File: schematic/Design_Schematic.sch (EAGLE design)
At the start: 8 parts, among them IC1 DS1307

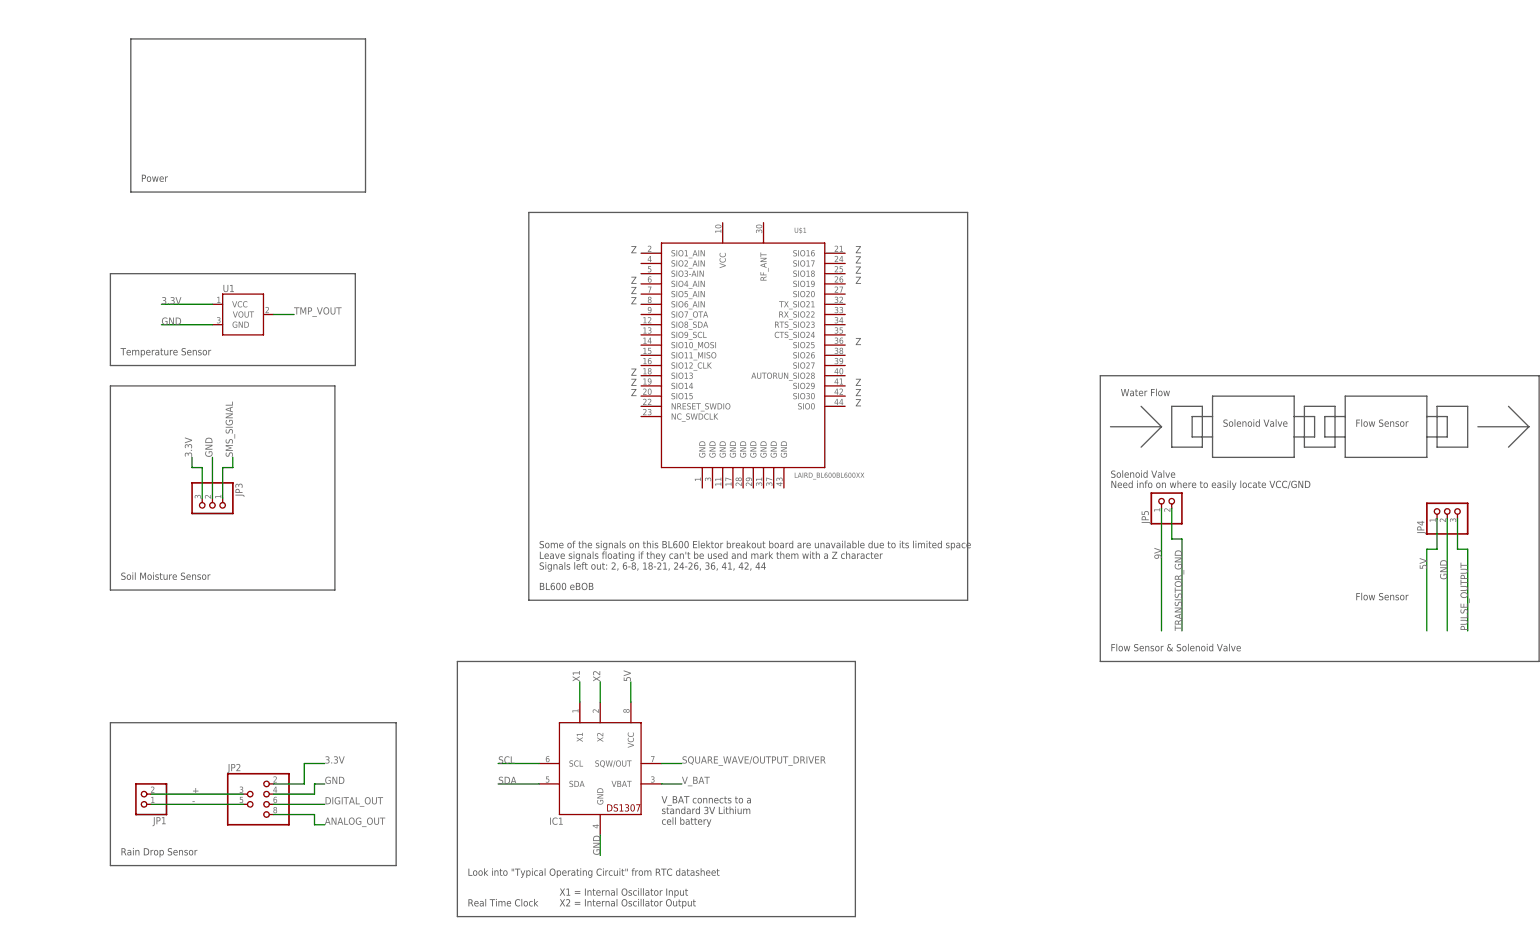
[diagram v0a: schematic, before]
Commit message: Updated schematic. Added connections
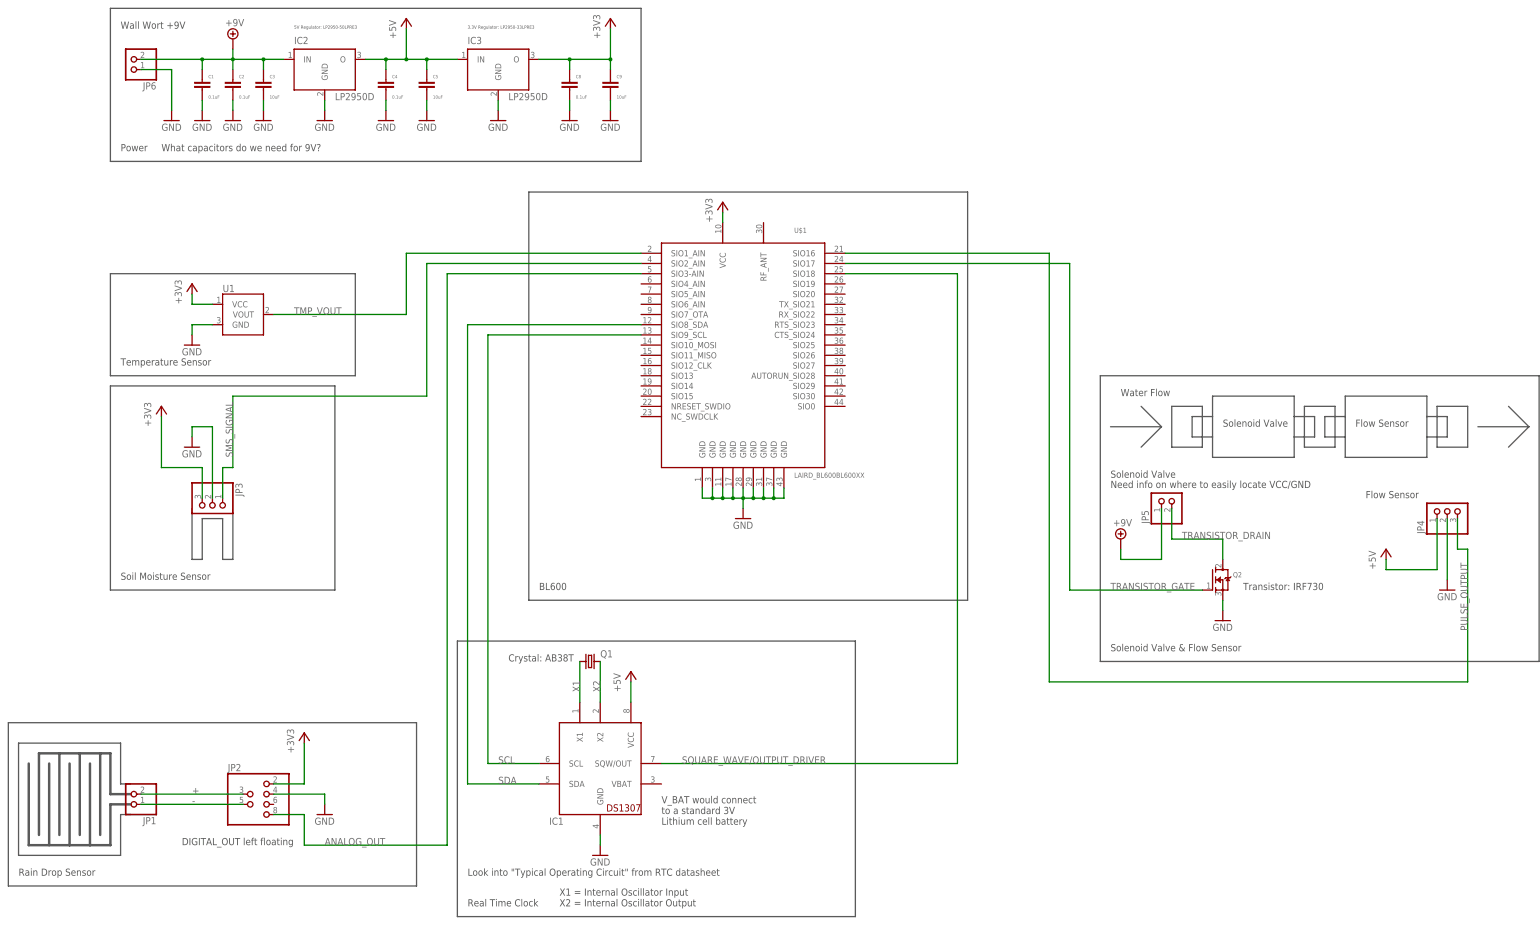
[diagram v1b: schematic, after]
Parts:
- added C1, C2, C4, C8: 0.1uF, rcl:C-EUC0805
- added C3, C5, C9: 10uF, rcl:C-EUC0805
- added IC2, IC3: LP2950D, national-semiconductor:LP2950D
- added JP6: (no value), pinhead:PINHD-1X2
- added Q1: (no value), crystal:CRYSTALTC38H
- added Q2: (no value), adafruit:MOSFET-NGDS_TO220V
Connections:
- removed net 3.3V: JP2.2, JP3.3, U1.VCC
- removed net 5V: IC1.VCC
- removed net 9V: JP5.2
- removed net DIGITAL_OUT: JP2.6
- removed net N$1: JP4.1
- removed net N$2: JP4.2
- removed net TRANSISTOR_GND: JP5.1
- removed net V_BAT: IC1.VBAT
- new net +3V3: C8.1, C9.1, IC3.O, JP2.2, JP3.3, U$1.VCC, U1.VCC
- new net +5V: C4.1, C5.1, IC1.VCC, IC2.O, IC3.IN, JP4.1
- new net +9V: C1.1, C2.1, C3.1, IC2.IN, JP5.1, JP6.2
- new net TRANSISTOR_DRAIN: JP5.2, Q2.D
- new net TRANSISTOR_GATE: Q2.G, U$1.SIO17
- net ANALOG_OUT: now also U$1.SIO3-AIN
- net GND: now also C1.2, C2.2, C3.2, C4.2, C5.2, C8.2, C9.2, IC2.GND, IC3.GND, JP4.2, JP6.1, Q2.S, U$1.GND, U$1.GND@1, U$1.GND@2, U$1.GND@3, U$1.GND@4, U$1.GND@5, U$1.GND@6, U$1.GND@7, U$1.GND@8
- net N$3: now also U$1.SIO16
- net SCL: now also U$1.SIO9_SCL
- net SDA: now also U$1.SIO8_SDA
- net SMS_SIGNAL: now also U$1.SIO2_AIN
- net SQUARE_WAVE: now also U$1.SIO18
- net TMP_VOUT: now also U$1.SIO1_AIN
- net X1: now also Q1.1
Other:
- note added: "3.3V Regulator: LP2950-33LPRE3"
- note added: "5V Regulator: LP2950-50LPRE3"
- note added: "BL600"
- note added: "Crystal: AB38T"
- note added: "DIGITAL_OUT left floating"
- note added: "Solenoid Valve & Flow Sensor"
- note added: "TRANSISTOR_DRAIN"
- note added: "TRANSISTOR_GATE"
- note added: "Transistor: IRF730"
- note added: "V_BAT would connect to a standard 3V Lithium cell battery"
- note added: "Wall Wort +9V"
- note added: "What capacitors do we need for 9V?"
- note removed: "3.3V"
- note removed: "5V"
- note removed: "9V"
- note removed: "BL600 eBOB"
- note removed: "DIGITAL_OUT"
- note removed: "Flow Sensor & Solenoid Valve"
- note removed: "GND"
- note removed: "Some of the signals on this BL600 Elektor breakout board are unavailable due to its limited space Leave signals floating if they can't be used and mark them with a Z character Signals left out: 2, 6-8, 18-21, 24-26, 36, 41, 42, 44"
- note removed: "TRANSISTOR_GND"
- note removed: "V_BAT"
- note removed: "V_BAT connects to a standard 3V Lithium cell battery"
- note removed: "Z"
- moved on the sheet: JP1

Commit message: Updated wiring
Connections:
- net +3V3: now also JP4.1
- net +5V: no longer JP4.1
- net N$3: now also U$1.SIO18; no longer U$1.SIO16
- net SQUARE_WAVE: now also U$1.SIO19; no longer U$1.SIO18
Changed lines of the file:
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@@
 <part name="P+1" library="supply1" deviceset="+5V" device=""/>
 <part name="Q1" library="crystal" deviceset="CRYSTAL" device="TC38H"/>
-<part name="P+3" library="supply1" deviceset="+5V" device=""/>
 <part name="GND15" library="supply1" deviceset="GND" device=""/>
 <part name="SUPPLY1" library="supply2" deviceset="+9V" device=""/>
@@
 <part name="+3V5" library="supply1" deviceset="+3V3" device=""/>
 <part name="GND17" library="supply1" deviceset="GND" device=""/>
+<part name="+3V6" library="supply1" deviceset="+3V3" device=""/>
 </parts>
 <sheets>
@@
 <instance part="P+1" gate="1" x="182.88" y="86.36"/>
 <instance part="Q1" gate="G$1" x="172.72" y="88.9"/>
-<instance part="P+3" gate="1" x="370.84" y="116.84"/>
 <instance part="GND15" gate="1" x="386.08" y="106.68"/>
 <instance part="SUPPLY1" gate="G$1" x="304.8" y="119.38"/>
@@
 <instance part="+3V5" gate="G$1" x="205.74" y="203.2"/>
 <instance part="GND17" gate="1" x="210.82" y="124.46"/>
+<instance part="+3V6" gate="G$1" x="370.84" y="116.84"/>
 </instances>
 <busses>
@@
 </segment>
 <segment>
-<wire x1="264.16" y1="185.42" x2="264.16" y2="63.5" width="0.1524" layer="91"/>
+<wire x1="264.16" y1="182.88" x2="264.16" y2="63.5" width="0.1524" layer="91"/>
 <wire x1="264.16" y1="63.5" x2="195.58" y2="63.5" width="0.1524" layer="91"/>
-<pinref part="U$1" gate="G$1" pin="SIO18"/>
-<wire x1="264.16" y1="185.42" x2="236.22" y2="185.42" width="0.1524" layer="91"/>
+<pinref part="U$1" gate="G$1" pin="SIO19"/>
+<wire x1="236.22" y1="182.88" x2="264.16" y2="182.88" width="0.1524" layer="91"/>
 </segment>
 </net>
@@
 <wire x1="391.16" y1="116.84" x2="391.16" y2="83.82" width="0.1524" layer="91"/>
 <wire x1="391.16" y1="83.82" x2="287.02" y2="83.82" width="0.1524" layer="91"/>
-<pinref part="U$1" gate="G$1" pin="SIO16"/>
-<wire x1="287.02" y1="83.82" x2="287.02" y2="190.5" width="0.1524" layer="91"/>
-<wire x1="287.02" y1="190.5" x2="236.22" y2="190.5" width="0.1524" layer="91"/>
+<wire x1="287.02" y1="83.82" x2="287.02" y2="185.42" width="0.1524" layer="91"/>
+<pinref part="U$1" gate="G$1" pin="SIO18"/>
+<wire x1="287.02" y1="185.42" x2="236.22" y2="185.42" width="0.1524" layer="91"/>
 </segment>
 </net>
@@
 <wire x1="182.88" y1="83.82" x2="182.88" y2="78.74" width="0.1524" layer="91"/>
 </segment>
-<segment>
-<pinref part="JP4" gate="A" pin="1"/>
-<wire x1="383.54" y1="124.46" x2="383.54" y2="111.76" width="0.1524" layer="91"/>
-<pinref part="P+3" gate="1" pin="+5V"/>
-<wire x1="383.54" y1="111.76" x2="370.84" y2="111.76" width="0.1524" layer="91"/>
-<wire x1="370.84" y1="111.76" x2="370.84" y2="114.3" width="0.1524" layer="91"/>
-</segment>
 </net>
 <net name="+3V3" class="0">
@@
 <wire x1="205.74" y1="200.66" x2="205.74" y2="198.12" width="0.1524" layer="91"/>
 </segment>
-</net>
+<segment>
+<pinref part="JP4" gate="A" pin="1"/>
+<wire x1="383.54" y1="124.46" x2="383.54" y2="111.76" width="0.1524" layer="91"/>
+<wire x1="383.54" y1="111.76" x2="370.84" y2="111.76" width="0.1524" layer="91"/>
+<wire x1="370.84" y1="111.76" x2="370.84" y2="114.3" width="0.1524" layer="91"/>
+<pinref part="+3V6" gate="G$1" pin="+3V3"/>
+</segment>
+</net>
